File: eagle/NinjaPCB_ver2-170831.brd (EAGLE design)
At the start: 71.7 x 53.2 mm, 65 parts, among them IC1 MCP3551SNNC, IC2 VNH5019/VNH3SP30NC, J2 WELL_TEMP, J3 HEATER, J4 HEATER_TEMP, J5 HEATER_TEMP, Q2 IRF520NPBF, Q3 IRF520NPBF, U1 CJT1117-3.3-SOT223

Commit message: fixing things
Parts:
- removed C3: (no value), rcl:E5-13
- added JP1: (no value), pinhead:2X02
- added JP3: (no value), pinhead:2X05
- moved SJ28 290.4 mm to (-99.1, 109.2)
- moved SJ27 288.3 mm to (-92.7, 109.2)
- moved SJ26 281.7 mm to (-86.4, 109.2)
- moved SJ25 272.0 mm to (-80.0, 109.2)
- moved SJ24 265.4 mm to (-73.7, 109.2)
- moved SJ22 265.4 mm to (-61.0, 109.2), turned to 0 degrees
- moved SJ33 253.5 mm to (-41.9, 114.3), turned to 0 degrees
- moved SJ34 249.2 mm to (-48.3, 114.3), turned to 0 degrees
- moved SJ32 247.5 mm to (-35.6, 114.3), turned to 0 degrees
- moved C2 246.7 mm to (-47.0, 105.4)
- moved SJ23 242.6 mm to (-67.3, 109.2)
- moved SJ18 242.1 mm to (-35.6, 109.2), turned to 0 degrees
- moved SJ31 238.6 mm to (-29.2, 114.3), turned to 0 degrees
- moved SJ17 236.3 mm to (-29.2, 109.2), turned to 0 degrees
- moved SJ21 235.3 mm to (-54.6, 109.2)
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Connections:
- removed net VCC: SJ16.1
- new net N$85: J2.2, JP1.4
- new net N$86: J2.1, JP1.2
- new net N$90: IC1.5, JP3.4
- new net N$91: IC1.6, JP3.6
- new net N$92: IC1.7, JP3.8
- net 12V: no longer C3.+
- net 3V3: now also JP3.1, JP3.2, SJ16.1
- net GND: now also JP1.3, JP3.10, JP3.9; no longer J2.2
- net GND1: no longer C3.-
- net N$1: now also JP1.1; no longer J2.1
- net SPI_CS: now also JP3.7; no longer IC1.7
- net SPI_SCK: now also JP3.3; no longer IC1.5
- net SPI_SDO: now also JP3.5; no longer IC1.6
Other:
- board size 71.7 x 53.2 mm -> 80 x 80 mm

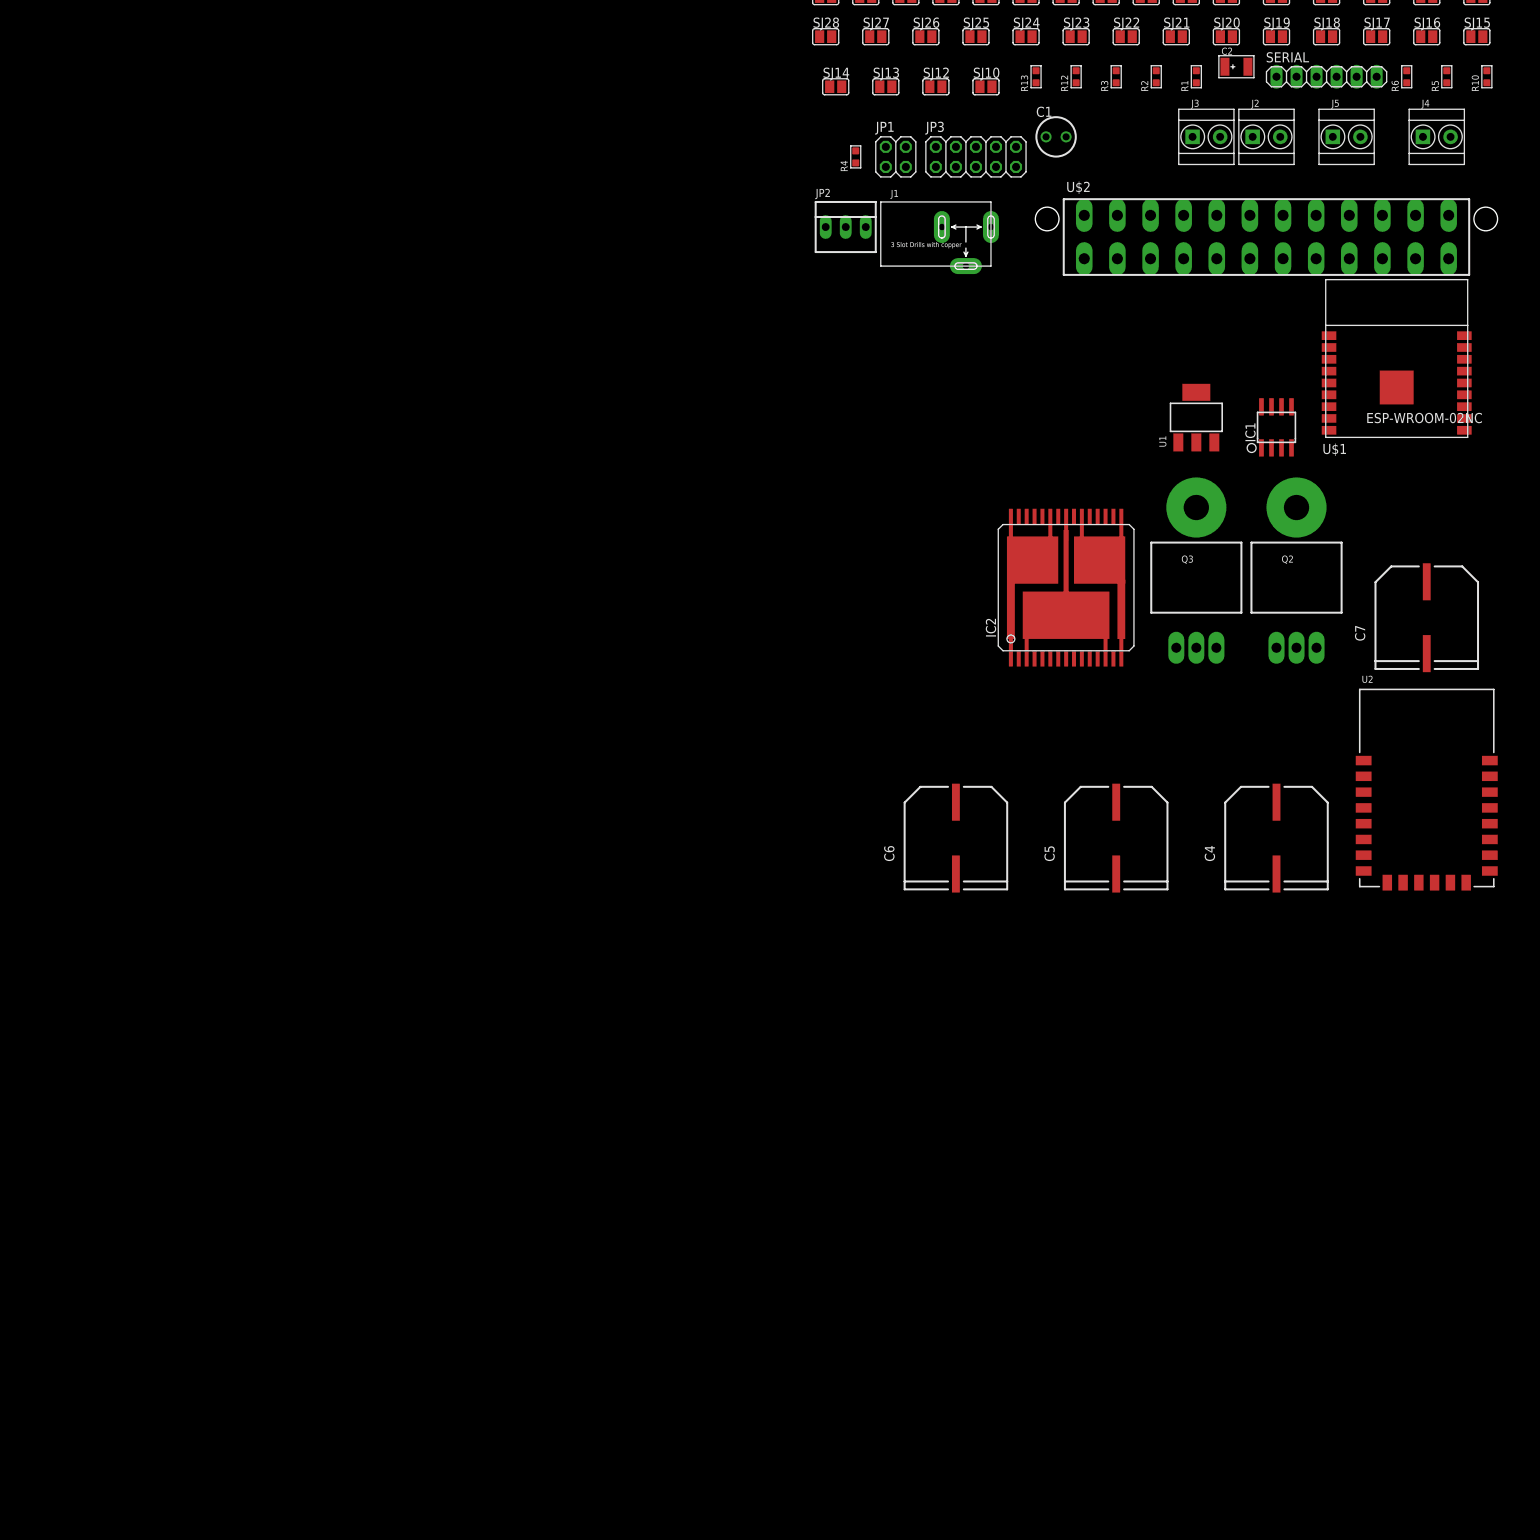
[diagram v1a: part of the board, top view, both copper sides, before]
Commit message: add evaluation board for NinjaPCB ver2
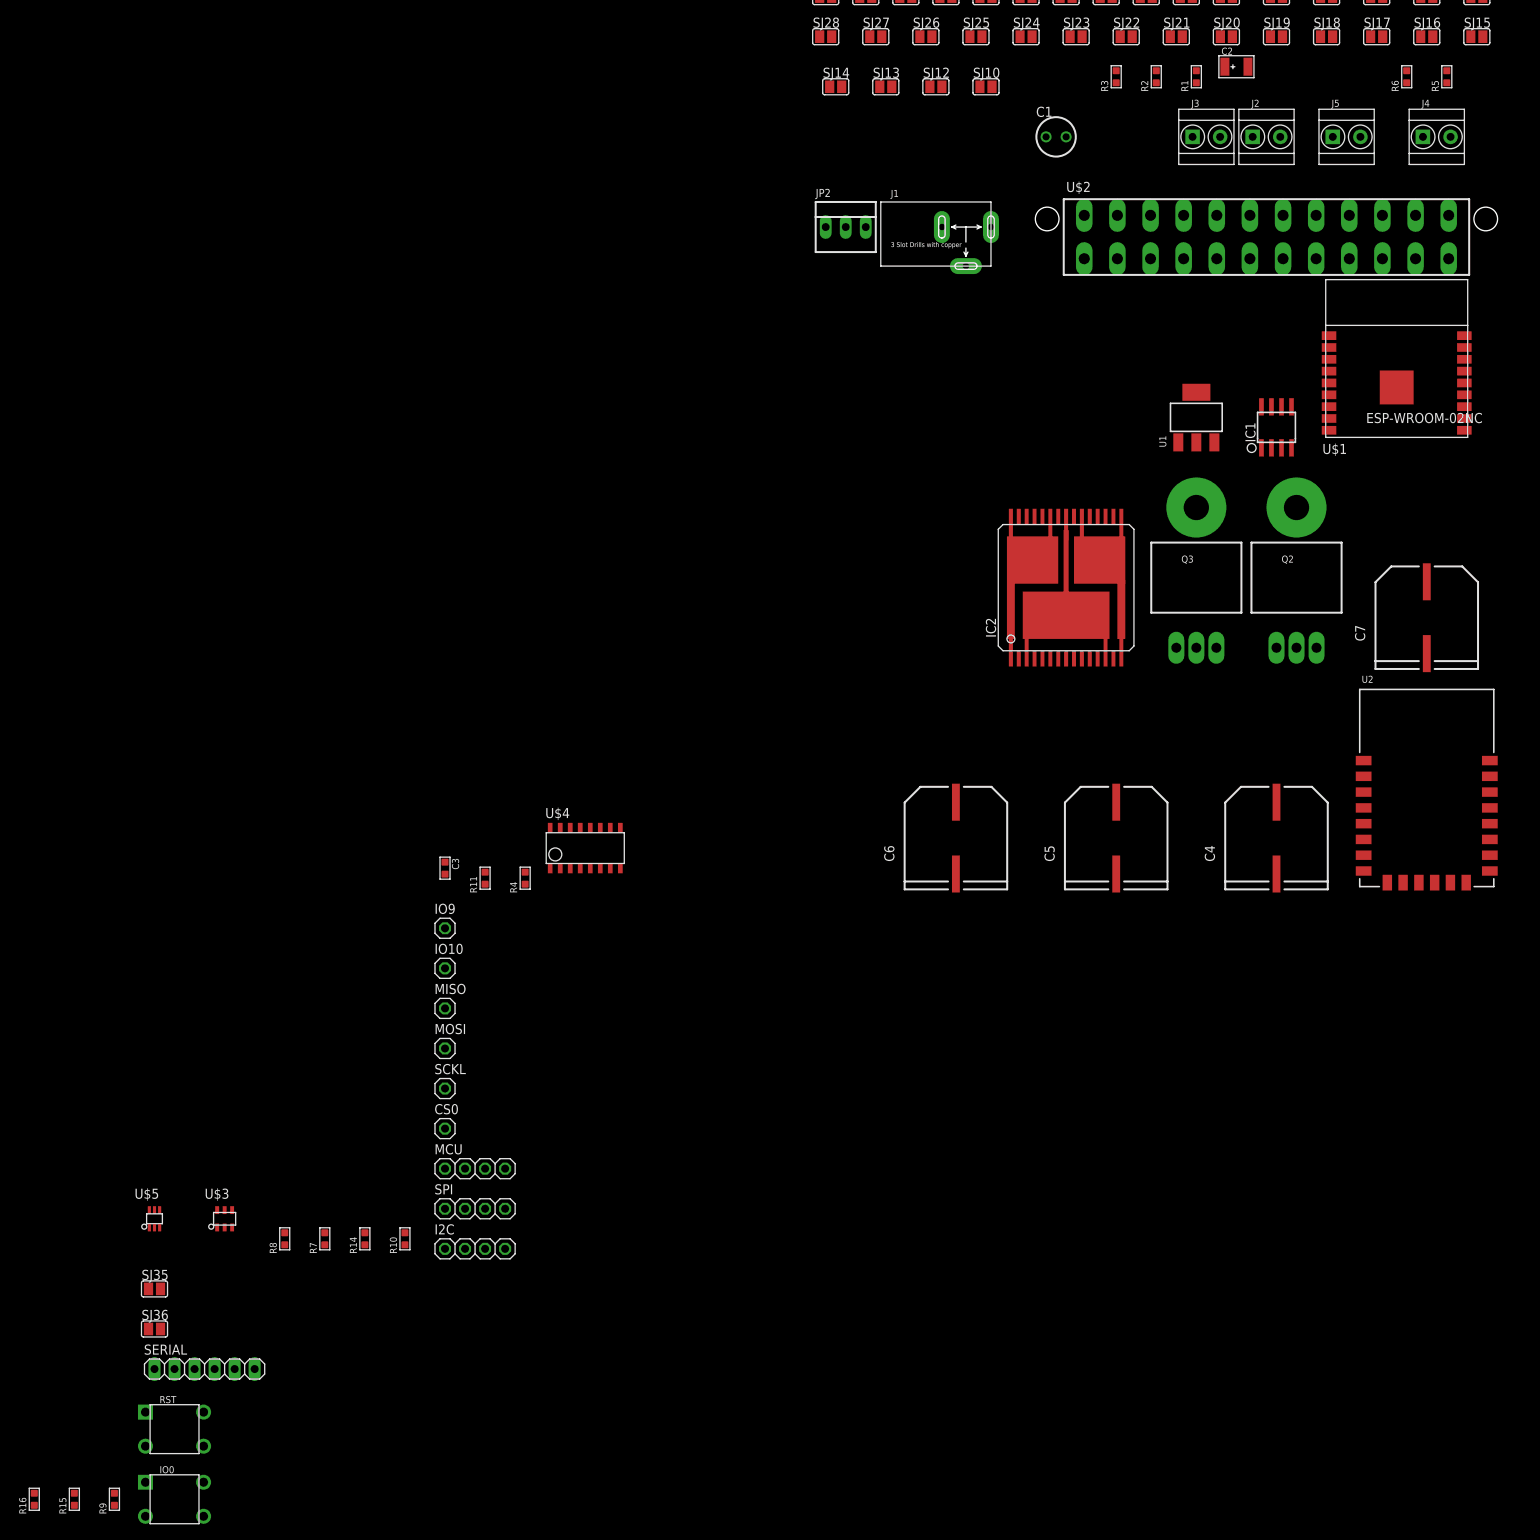
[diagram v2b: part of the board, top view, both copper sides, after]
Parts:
- removed JP1: (no value), pinhead:2X02
- removed JP3: (no value), pinhead:2X05
- removed R12, R13: 1K 1/10W, Seeed-Resistor:R0603
- added C3: 100nf, Seeed-Capacitor:C0603
- added CS0, IO10, IO9, MISO, MOSI, SCKL: (no value), pinhead:1X01
- added I2C, MCU, SPI: (no value), pinhead:1X04OCT
- added IO0, RST: (no value), Seeed-Switch:SW4-6.0X6.0X5.0MM
- added R11: 1.5K or 1.8K, Seeed-Resistor:R0603
- added R14: 2K, Seeed-Resistor:R0603
- added R15, R16, R9: 10K 1/10W, Seeed-Resistor:R0603
- added R7: 30K, Seeed-Resistor:R0603
- added R8: 15K 1/10W, Seeed-Resistor:R0603
- added SJ35, SJ36: (no value), jumper:SJ
- added U$3: ANALOGSW_AD_SOT23-6, PCR-IC:SOT-23-6
- added U$4: NAU7802, PCR-IC:SOP-16
- added U$5: ANALOGSW_TI-SC70-5/6, PCR-IC:SC70-6
- R10: value 1.5K or 1.8K -> 3K
- U2: value (none) -> ESP-12F
- moved SERIAL 217.0 mm to (-177.8, -59.7)
- moved R10 201.3 mm to (-152.4, -43.2)
- moved R4 100.6 mm to (-137.2, 2.54)
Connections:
- removed net N$26: SJ8.2
- removed net N$28: SJ10.2
- removed net N$30: SJ12.2
- removed net N$33: SJ14.2
- removed net N$34: SJ7.1
- removed net N$35: SJ6.1
- removed net N$36: SJ5.1
- removed net N$37: SJ4.1
- removed net N$38: SJ3.1
- removed net N$39: SJ2.1
- removed net N$41: SJ15.1
- removed net N$54: SJ24.2
- removed net N$55: SJ25.2
- removed net N$56: SJ26.2
- removed net N$57: SJ27.2
- removed net N$58: SJ28.2
- removed net N$59: SJ29.2
- removed net N$60: SJ30.2
- removed net N$74: SJ19.1
- removed net N$75: SJ20.1
- removed net N$76: SJ21.1
- removed net N$77: SJ22.1
- removed net N$78: SJ23.1
- removed net N$79: SERIAL.6
- removed net N$80: SERIAL.5
- removed net N$81: SERIAL.4
- removed net N$82: SERIAL.3
- removed net N$83: SERIAL.2
- removed net N$84: SERIAL.1
- removed net N$85: J2.2, JP1.4
- removed net N$86: J2.1, JP1.2
- removed net N$90: IC1.5, JP3.4
- new net EXTADC_I2C_SCL: I2C.1, U$4.P$13
- new net EXTADC_I2C_SDA: I2C.3, U$4.P$14
- new net EXTADC_RDY: I2C.4, U$4.P$12
- new net HIGH_TEMP: SJ23.1, SJ8.2, U$3.P$4, U$5.P$4
- new net IO12: MCU.2, SJ19.1, SJ3.1
- new net IO14: MCU.1, SJ2.1, SJ21.1
- new net IO2: MCU.3, SJ27.2, SJ6.1
- new net IO5: MCU.4, SJ11.2, SJ29.2
- new net RESET: R9.2, RST.1, RST.4, SJ10.2, SJ15.1
- new net RXD: SERIAL.2, SJ13.2, SJ25.2
- new net TXD: SERIAL.3, SJ12.2, SJ24.2
- new net VCC: R9.1
- new net WELL_TEMP: J2.1, R7.1, R8.2, SJ35.2, SJ36.2
- net 3V3: now also J4.1, R4.2, R7.2, U$3.P$1, U$3.P$6, U$4.P$1, U$4.P$15, U$4.P$16, U$5.P$1, U$5.P$6; no longer JP3.1, JP3.2, R10.2, R4.1
- net FAN: now also R15.1, SJ20.1, SJ4.1; no longer R13.1
- net GND: now also C3.1, IO0.2, IO0.3, J2.2, R11.1, R14.2, RST.2, RST.3, SERIAL.6, U$3.P$3, U$4.P$7, U$4.P$8, U$4.P$9, U$5.P$3; no longer J4.2, JP1.3, JP3.10, JP3.9
- net HEATER: now also R16.1, SJ22.1, SJ5.1; no longer R12.1
- net INT_ADC: now also R14.1, SJ30.2, SJ9.2; no longer J4.1
- net N$1: now also J4.2, R10.2; no longer IC1.2, JP1.1, R4.2
- net N$27: now also R8.1, U$3.P$2, U$5.P$2; no longer SJ9.2
- net N$29: now also SJ36.1, U$4.P$3; no longer SJ11.2
- net N$3: now also R16.2; no longer R12.2
- net N$31: now also IC1.2, SJ35.1; no longer SJ13.2
- net N$5: now also R15.2; no longer R13.2
- net N$61: now also MISO.1
- net N$62: now also MOSI.1
- net N$63: now also SCKL.1
- net N$64: now also CS0.1
- net N$72: now also IO9.1
- net N$73: now also IO10.1
- net N$91: now also R11.2, R4.1, U$4.P$2; no longer IC1.6, JP3.6
- net N$92: now also C3.2, U$4.P$6; no longer IC1.7, JP3.8
- net PEL_INA: now also I2C.2, SPI.3
- net PEL_INB: now also IO0.1, IO0.4, SJ26.2, SJ7.1
- net PEL_PWM: now also SJ14.2, SJ28.2
- net SPI_CS: now also IC1.7, SPI.4; no longer JP3.7
- net SPI_SCK: now also IC1.5, SPI.1; no longer JP3.3
- net SPI_SDO: now also IC1.6, SPI.2; no longer JP3.5

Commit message: completed ver2-170831
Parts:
- removed C1: CAP_TH_10UF_50V, Seeed-OPL-2017-01-Capacitor-akita:CAP_TH_P25_D50_POL
- removed C4, C5, C6: CAP_SMDAL_1000UF_25V, Seeed-OPL-2017-01-Capacitor-akita:CAP_SMD_AL_D125
- removed I2C, MCU, SPI: (no value), pinhead:1X04OCT
- removed IC1: MCP3551SNNC, microchip:SO-08-NOCREAM
- removed R7: 30K, Seeed-Resistor:R0603
- removed R8: 15K 1/10W, Seeed-Resistor:R0603
- removed SJ18, SJ31, SJ32, SJ33, SJ34, SJ35, SJ36: (no value), jumper:SJ
- removed U$1: ESP-WROOM-02NC, PCR-Module:ESP-WROOM-02-NOCREAM
- removed U$2: ATX24, PCR-Connector:ATX24
- removed U$3: ANALOGSW_AD_SOT23-6, PCR-IC:SOT-23-6
- removed U$4: NAU7802, PCR-IC:SOP-16
- removed U$5: ANALOGSW_TI-SC70-5/6, PCR-IC:SC70-6
- removed U2: ESP-12F, Seeed-OPL-2017-01-Sensor-camilo:ESP-12F
- added C8: CAP_E5-13-L3030RINV, PCR-RCL:E5-13-L30R-INV
- added ESP1: ESP-WROOM-02NC, PCR-Module:ESP-WROOM-02-NOCREAM
- added ESP2: ESP-12F, Seeed-OPL-2017-01-Sensor-camilo:ESP-12F
- added IC3: ANALOGSW_AD_SOT23-6NC, PCR-IC:SOT-23-6NC
- added IC4: ANALOGSW_TI-SC70-5/6NC, PCR-IC:SC70-6NC
- added IC5: MCP3551SNNC, microchip:SO-08-NOCREAM
- added IC6: NAU7802NC, PCR-IC:SOP-16NC
- added MODE: (no value), Seeed-Switch:SW4-6.0X6.0X5.0MM
- added R12: 10K 1/10W, Seeed-Resistor:R0603
- added RH: 15K 1/10W, PCR-RCL:R0603NC
- added RL: 30K, PCR-RCL:R0603NC
- added SJ37, SJ38, SJ39, SJ40: (no value), jumper:SJ_2
- added WELLEXT1, WELLEXT2, WELL_TEMP: (no value), pinhead:1X02
- IC2: value VNH5019/VNH3SP30NC -> VNH5019/VNH3SP30-BNC; device st-microelectronics:MULTIPOWERSO-30-NOCREAM -> st-microelectronics:MULTIPOWERSO-30-B-NOCREAM
- J2: value WELL_TEMP -> ATX24; device Seeed-Connector:H2-3.5-7.0X7.0MM -> PCR-Connector:ATX24
- J5: value HEATER_TEMP -> PELTIER
- R11, R4: device Seeed-Resistor:R0603 -> PCR-RCL:R0603NC
- SJ17: device jumper:SJ -> jumper:SJ_2
- moved R16 250.3 mm to (44.0, -17.8)
- moved SERIAL 246.9 mm to (69.0, -65.0), flipped to the bottom, turned to 90 degrees
- moved R15 246.6 mm to (45.3, -17.8)
- moved SJ9 230.0 mm to (51.9, -59.2), flipped to the bottom, turned to 270 degrees
- moved IO0 229.7 mm to (48.0, -70.0), flipped to the bottom, turned to 180 degrees
- moved SJ14 229.5 mm to (64.6, -59.2), flipped to the bottom, turned to 270 degrees
- moved SJ28 228.7 mm to (57.0, -58.0), turned to 270 degrees
- moved SJ8 225.1 mm to (49.4, -59.2), flipped to the bottom, turned to 270 degrees
- moved SJ13 223.3 mm to (62.1, -59.2), flipped to the bottom, turned to 270 degrees
- moved R9 221.1 mm to (31.3, -61.3), turned to 180 degrees
- moved SJ27 221.1 mm to (51.9, -58.0), turned to 270 degrees
- moved RST 219.6 mm to (38.0, -70.0), flipped to the bottom, turned to 180 degrees
- moved SJ25 219.4 mm to (62.1, -58.0), turned to 270 degrees
- moved SJ26 218.6 mm to (54.5, -58.0), turned to 270 degrees
- moved SJ12 217.2 mm to (59.5, -59.2), flipped to the bottom, turned to 270 degrees
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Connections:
- removed net GND1: IC2.18, IC2.19, IC2.20, IC2.26, IC2.27, IC2.28
- removed net N$25: IC2.1, IC2.25, IC2.30, IC2.OUTA, IC2.OUTA@1, J5.1
- removed net N$29: SJ36.1, U$4.P$3
- removed net N$31: IC1.2, SJ35.1
- removed net N$32: IC2.15, IC2.16, IC2.21, IC2.OUTB, IC2.OUTB@1, J5.2
- removed net N$50: SJ31.1, U2.10
- removed net N$51: SJ32.1, U2.13
- removed net N$52: SJ33.1, U2.14
- removed net N$53: SJ34.1, U2.9
- removed net N$65: SJ17.2, U2.11
- removed net N$66: SJ18.2, U2.12
- removed net VCC: R9.1
- new net I2C_WELL_TEMP: IC6.P$3, SJ17.3
- new net N$26: WELLEXT1.1, WELLEXT2.1
- new net N$28: WELLEXT1.2, WELLEXT2.2
- new net OUTA: IC2.25, IC2.30, IC2.OUTA, J5.1
- new net OUTB: IC2.15, IC2.16, IC2.21, IC2.OUTB, J5.2
- new net SPI_WELL_TEMP: IC5.2, SJ17.1
- net 12V: now also C8.+, J2.10, J2.11; no longer C1.P$P, C4.P$P, C5.P$P, C6.P$P, IC2.VCC@1, U$2.10, U$2.11
- net 3V3: now also IC3.P$1, IC3.P$6, IC4.P$1, IC4.P$6, IC5.1, IC5.8, IC6.P$1, IC6.P$15, IC6.P$16, J4.2, MODE.1, MODE.4, R9.1, RL.2; no longer IC1.1, IC1.8, J4.1, R7.2, U$3.P$1, U$3.P$6, U$4.P$1, U$4.P$15, U$4.P$16, U$5.P$1, U$5.P$6
- net EXTADC_I2C_SCL: now also IC6.P$13, SJ37.3; no longer I2C.1, U$4.P$13
- net EXTADC_I2C_SDA: now also IC6.P$14, SJ39.3; no longer I2C.3, U$4.P$14
- net EXTADC_RDY: now also IC6.P$12, SJ40.3; no longer I2C.4, U$4.P$12
- net GND: now also C8.-, ESP1.P$13, ESP1.P$18, ESP1.P$19, ESP1.P$9, ESP2.15, IC2.18, IC2.19, IC2.20, IC2.26, IC2.27, IC2.28, IC3.P$3, IC4.P$3, IC5.3, IC5.4, IC6.P$7, IC6.P$8, IC6.P$9, J1.-2, J2.15, J2.17, J2.18, J2.19, J2.24, J2.3, J2.5, J2.7, R12.1, WELL_TEMP.2; no longer C1.P$M, C4.P$M, C5.P$M, C6.P$M, IC1.3, IC1.4, J2.2, U$1.P$13, U$1.P$18, U$1.P$19, U$1.P$9, U$2.15, U$2.17, U$2.18, U$2.19, U$2.24, U$2.3, U$2.5, U$2.7, U$3.P$3, U$4.P$7, U$4.P$8, U$4.P$9, U$5.P$3, U2.15
- net HIGH_TEMP: now also IC3.P$4, IC4.P$4, MODE.2, MODE.3, R12.2; no longer U$3.P$4, U$5.P$4
- net IO12: now also SJ38.2; no longer MCU.2
- net IO14: now also SJ37.2; no longer MCU.1
- net IO2: now also SJ39.2; no longer MCU.3
- net IO5: now also SJ40.2; no longer MCU.4
- net N$1: now also J4.1; no longer J4.2
- net N$11: now also ESP1.P$1, ESP1.P$2; no longer U$1.P$1, U$1.P$2
- net N$12: now also ESP1.P$3; no longer U$1.P$3
- net N$13: now also ESP1.P$4; no longer U$1.P$4
- net N$14: now also ESP1.P$5; no longer U$1.P$5
- net N$15: now also ESP1.P$6; no longer U$1.P$6
- net N$16: now also ESP1.P$7; no longer U$1.P$7
- net N$17: now also ESP1.P$8; no longer U$1.P$8
- net N$18: now also ESP1.P$17; no longer U$1.P$17
- net N$19: now also ESP1.P$16; no longer U$1.P$16
- net N$20: now also ESP1.P$15; no longer U$1.P$15
- net N$21: now also ESP1.P$14; no longer U$1.P$14
- net N$22: now also ESP1.P$12; no longer U$1.P$12
- net N$23: now also ESP1.P$11; no longer U$1.P$11
- net N$24: now also ESP1.P$10; no longer U$1.P$10
- net N$27: now also IC3.P$2, IC4.P$2, RH.1; no longer R8.1, U$3.P$2, U$5.P$2
- net N$40: now also ESP2.1; no longer U2.1
- net N$42: now also ESP2.3, ESP2.8; no longer U2.3, U2.8
- net N$43: now also ESP2.22; no longer U2.22
- net N$44: now also ESP2.21; no longer U2.21
- net N$45: now also ESP2.18; no longer U2.18
- net N$46: now also ESP2.17; no longer U2.17
- net N$47: now also ESP2.19; no longer U2.19
- net N$48: now also ESP2.20; no longer U2.20
- net N$49: now also ESP2.2; no longer U2.2
- net N$61: now also ESP2.10; no longer SJ31.2
- net N$62: now also ESP2.13; no longer SJ32.2
- net N$63: now also ESP2.14; no longer SJ33.2
- net N$64: now also ESP2.9; no longer SJ34.2
- net N$67: now also ESP2.6; no longer U2.6
- net N$68: now also ESP2.7; no longer U2.7
- net N$69: now also ESP2.5; no longer U2.5
- net N$70: now also ESP2.16; no longer U2.16
- net N$71: now also ESP2.4; no longer U2.4
- net N$72: now also ESP2.11; no longer SJ17.1
- net N$73: now also ESP2.12; no longer SJ18.1
- net N$91: now also IC6.P$2; no longer U$4.P$2
- net N$92: now also IC6.P$6; no longer U$4.P$6
- net PEL_INA: now also SJ38.3, SJ39.1; no longer I2C.2, SPI.3
- net SPI_CS: now also IC5.7, SJ40.1; no longer IC1.7, SPI.4
- net SPI_SCK: now also IC5.5, SJ37.1; no longer IC1.5, SPI.1
- net SPI_SDO: now also IC5.6, SJ38.1; no longer IC1.6, SPI.2
- net WELL_TEMP: now also RH.2, RL.1, SJ17.2, WELL_TEMP.1; no longer J2.1, R7.1, R8.2, SJ35.2, SJ36.2
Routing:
- net GND: track 0.00 -> 682.9 mm, vias 0 -> 69
- net 12V: track 0.00 -> 289.6 mm, vias 0 -> 45
- net 3V3: track 0.00 -> 239.5 mm, vias 0 -> 8
- net PEL_INB: track 0.00 -> 151.9 mm, vias 0 -> 3
- net HIGH_TEMP: track 0.00 -> 123.2 mm, vias 0 -> 5
- net RESET: track 0.00 -> 98.8 mm, vias 0 -> 2
- net INT_ADC: track 0.00 -> 96.3 mm, vias 0 -> 1
- net HEATER: track 0.00 -> 91.8 mm, vias 0 -> 2
- net OUTB: track 0.00 -> 89.9 mm, vias 0 -> 16
- net IO2: track 0.00 -> 85.7 mm, vias 0 -> 2
- net PEL_PWM: track 0.00 -> 83.9 mm, vias 0 -> 2
- net IO5: track 0.00 -> 75.0 mm, vias 0 -> 2
- net OUTA: track 0.00 -> 65.3 mm, vias 0 -> 26
- net N$1: track 0.00 -> 45.5 mm, vias 0 -> 1
- net WELL_TEMP: track 0.00 -> 39.6 mm
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- added copper zone on layer 1, net 12V
- added copper zone on layer 16, net 12V
- added copper zone on layer 1, net GND
- added copper zone on layer 16, net GND
- added copper zone on layer 1, net OUTA
- added copper zone on layer 16, net OUTA
- added copper zone on layer 16, net OUTB
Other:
- board size 80 x 80 mm -> 72 x 79 mm
- board text added: "ESP -WROOM-02"
- board text added: "ESP-12F"
- board text added: "FAN"
- board text added: "GND"
- board text added: "HEATER"
- board text added: "HEATER_TEMP"
- board text added: "I2C"
- board text added: "J1"
- board text added: "J3"
- board text added: "J4"
- board text added: "J5"
- board text added: "JP2"
- board text added: "NinjaPCB ver2-170831"
- board text added: "PELTIER"
- board text added: "Q2"
- board text added: "Q3"
- board text added: "RX"
- board text added: "SPI"
- board text added: "TX"
- board text added: "WELL_TEMP"

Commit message: completed ver2-170831
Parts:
- removed J1: (no value), Seeed-Connector:3P-L14.2*W11.0*H9.0MM
- added U$1: 2.1MMJACKTHM, adafruit:PJ-102A
- moved WELLEXT1 97.3 mm to (66.3, -76.1)
- moved WELLEXT2 95.6 mm to (70.1, -76.1)
- moved J5 3.03 mm to (12.9, -13.5), turned to 90 degrees
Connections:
- net 12V: now also U$1.TIP; no longer J1.+
- net GND: now also U$1.RING, U$1.RING_SW; no longer J1.-1, J1.-2
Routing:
- net GND: track 682.9 -> 700.9 mm
- net 12V: track 289.6 -> 296.9 mm
- net OUTA: track 65.3 -> 60.7 mm
- net N$28: track 6.35 -> 3.81 mm
- net N$26: track 6.35 -> 3.81 mm
- net OUTB: track 89.9 -> 91.9 mm
